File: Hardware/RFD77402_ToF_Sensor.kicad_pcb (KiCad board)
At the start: 2 copper layers, 25.4 x 25.4 mm, 18 parts, among them J1 QWIIC_CONNECTORJS-1MM, J2 QWIIC_CONNECTORJS-1MM, J3 CONN_01, J4 I2C_STANDARD, U1 RFD77402, U4 CC_LICENSE

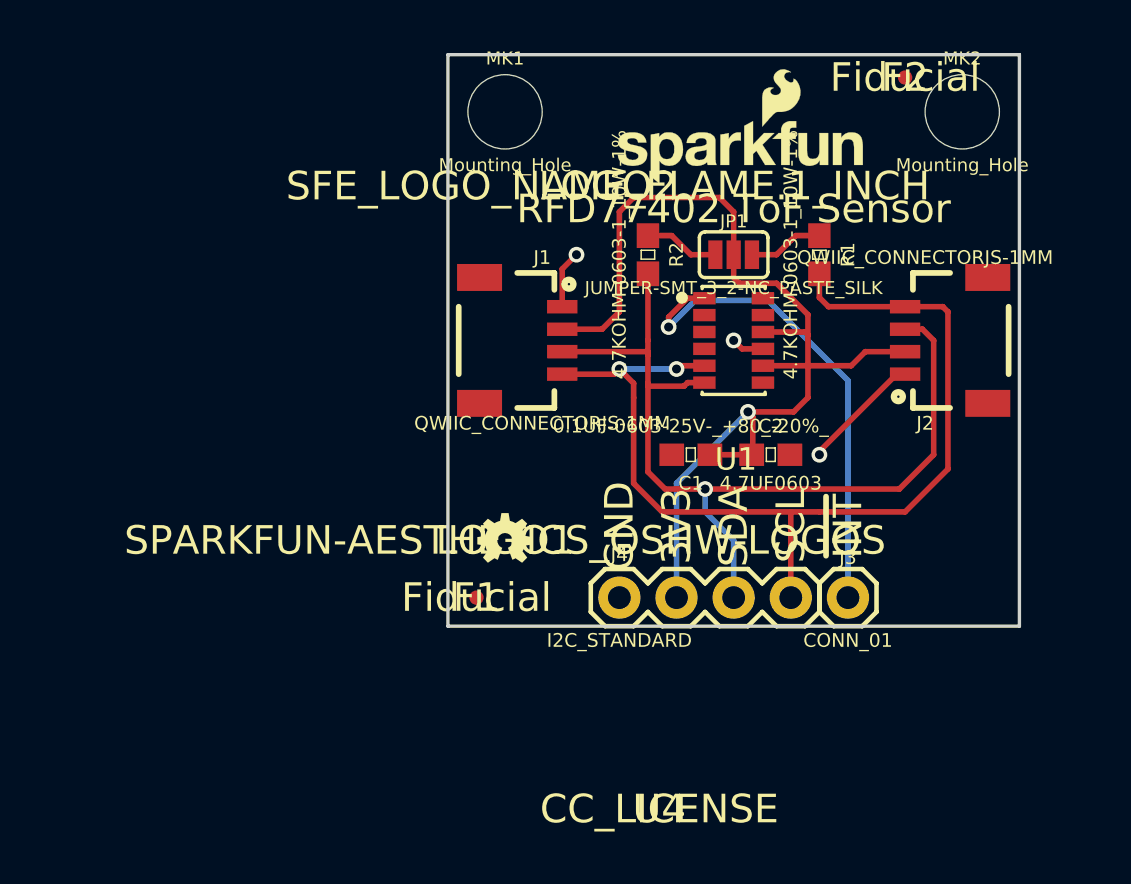
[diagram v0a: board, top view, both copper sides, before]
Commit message: Added fiducials
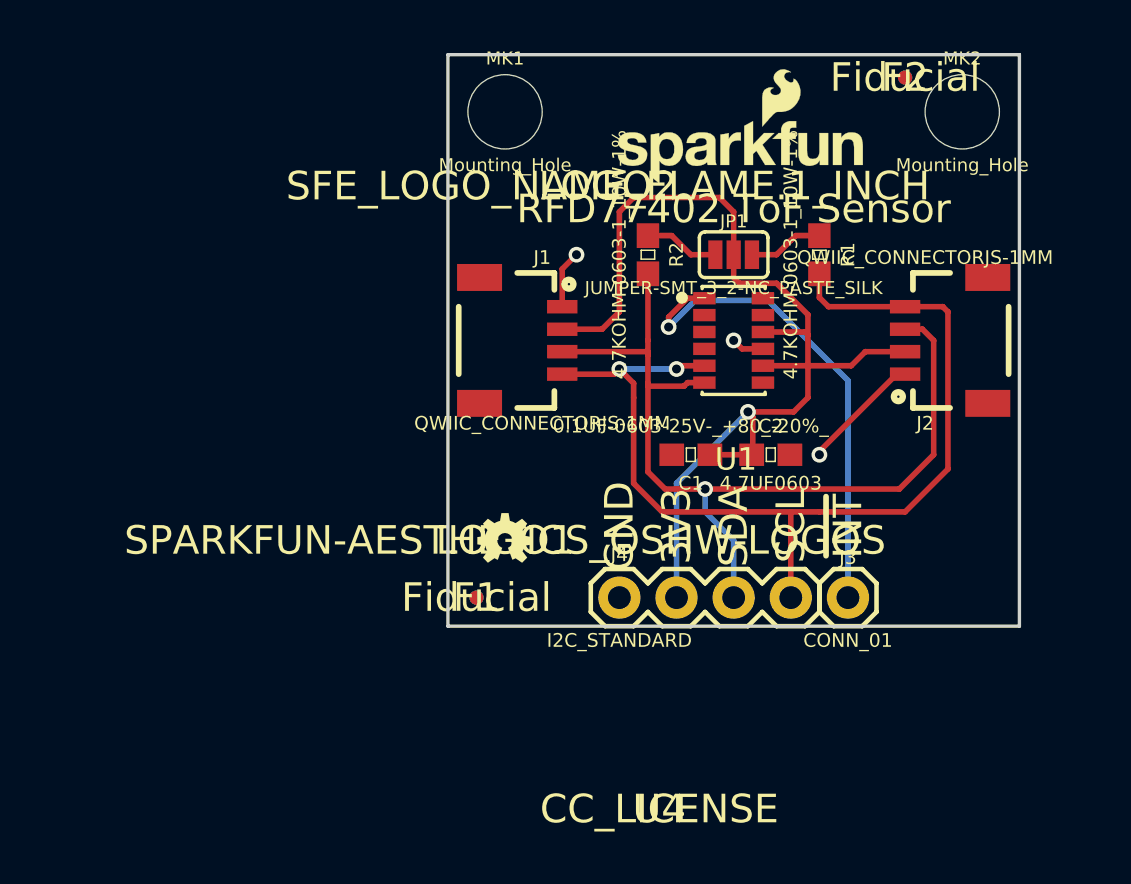
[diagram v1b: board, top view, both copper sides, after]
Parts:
- added F3: Fiducial, Aesthetics:FIDUCIAL-MICRO, B.Cu at (138.4, 115.6)
- added F4: Fiducial, Aesthetics:FIDUCIAL-MICRO, B.Cu at (157.5, 92.5)
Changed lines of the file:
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@@
     (tracks 96)
     (zones 0)
-    (modules 18)
+    (modules 20)
     (nets 8)
   )
@@
     (pad_to_mask_clearance 0.075)
     (aux_axis_origin 0 0)
-    (visible_elements 7FFCF3E9)
+    (visible_elements 7FFCF7E9)
     (pcbplotparams
       (layerselection 0x00030_80000001)
@@
       (net 1 GND))
   )
+  (module Aesthetics:FIDUCIAL-MICRO (layer B.Cu)
+    (at 138.43 115.57)
+    (descr "FIDUCIAL - CIRCLE, 0.25IN")
+    (tags "FIDUCIAL - CIRCLE, 0.25IN")
+    (attr smd)
+    (fp_text reference F3 (at 0 0) (layer B.SilkS)
+      (effects (font (thickness 0.15)) (justify mirror))
+    )
+    (fp_text value Fiducial (at 0 0) (layer B.SilkS)
+      (effects (font (thickness 0.15)) (justify mirror))
+    )
+    (pad 1 smd circle (at 0 0) (size 0.635 0.635) (layers B.Cu B.Paste B.Mask)
+      (solder_mask_margin 0.1016))
+  )
+  (module Aesthetics:FIDUCIAL-MICRO (layer B.Cu)
+    (at 157.48 92.456)
+    (descr "FIDUCIAL - CIRCLE, 0.25IN")
+    (tags "FIDUCIAL - CIRCLE, 0.25IN")
+    (attr smd)
+    (fp_text reference F4 (at 0 0) (layer B.SilkS)
+      (effects (font (thickness 0.15)) (justify mirror))
+    )
+    (fp_text value Fiducial (at 0 0) (layer B.SilkS)
+      (effects (font (thickness 0.15)) (justify mirror))
+    )
+    (pad 1 smd circle (at 0 0) (size 0.635 0.635) (layers B.Cu B.Paste B.Mask)
+      (solder_mask_margin 0.1016))
+  )
   (gr_text "RFD77402 ToF Sensor" (at 149.86 98.298) (layer B.SilkS)

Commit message: Post design review changes
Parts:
- added GND: VIA-15mil, Hardware:VIA-15mil, F.Cu at (159.8, 112.5)
- moved C1 1.53 mm to (147.8, 107.7)
- moved C2 1.53 mm to (151.4, 107.7)
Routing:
- net +3V3: track 48.5 -> 57.5 mm, vias 1 -> 2
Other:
- board text added: "Designed By: Nate Seidle Revised By: Andy England"
- board text added: "PU"
- board text added: "v01"
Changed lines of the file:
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@@
 (kicad_pcb (version 4) (host pcbnew 4.0.7)
   (general
-    (links 24)
+    (links 25)
     (no_connects 0)
-    (area 137.084999 91.364999 162.635001 116.915001)
+    (area 117.656001 90.922499 173.827142 126.4622)
     (thickness 1.6)
-    (drawings 16)
-    (tracks 96)
+    (drawings 22)
+    (tracks 104)
     (zones 0)
-    (modules 20)
+    (modules 21)
     (nets 8)
   )
@@
     (39 F.Mask user)
     (44 Edge.Cuts user)
-    (46 B.CrtYd user hide)
-    (47 F.CrtYd user hide)
+    (46 B.CrtYd user)
+    (47 F.CrtYd user)
     (48 B.Fab user hide)
     (49 F.Fab user)
@@
     (mod_text_size 1 1)
     (mod_text_width 0.15)
-    (pad_size 1.524 1.524)
-    (pad_drill 0.762)
+    (pad_size 0.6 0.6)
+    (pad_drill 0.3)
     (pad_to_mask_clearance 0.075)
     (aux_axis_origin 0 0)
-    (visible_elements 7FFCF7E9)
+    (visible_elements 7FFCFFEF)
     (pcbplotparams
       (layerselection 0x00030_80000001)
@@
   )
   (module Capacitors:0603 (layer F.Cu)
-    (at 147.955 109.22 180)
+    (at 147.828 107.696 180)
     (descr "GENERIC 1608 (0603) PACKAGE")
     (tags "GENERIC 1608 (0603) PACKAGE")
@@
   )
   (module Capacitors:0603 (layer F.Cu)
-    (at 151.51 109.22)
+    (at 151.384 107.696)
     (descr "GENERIC 1608 (0603) PACKAGE")
     (tags "GENERIC 1608 (0603) PACKAGE")
@@
       (solder_mask_margin 0.1016))
   )
+  (module Hardware:VIA-15mil (layer F.Cu)
+    (at 159.766 112.522)
+    (fp_text reference GND (at 0 0.5) (layer F.SilkS)
+      (effects (font (size 1 1) (thickness 0.15)))
+    )
+    (fp_text value VIA-15mil (at 0 -0.5) (layer F.Fab)
+      (effects (font (size 1 1) (thickness 0.15)))
+    )
+    (pad 1 thru_hole circle (at 0 0) (size 0.6 0.6) (drill 0.3) (layers *.Cu)
+      (net 1 GND) (zone_connect 2))
+  )
+  (gr_text PU (at 147.574 100.33 90) (layer F.SilkS)
+    (effects (font (size 1 1) (thickness 0.25)))
+  )
+  (gr_text "Designed By: Nate Seidle\nRevised By: Andy England" (at 148.844 121.412) (layer F.Fab)
+    (effects (font (size 1.27 1.27) (thickness 0.254)))
+  )
+  (dimension 25.4 (width 0.254) (layer F.Fab)
+    (gr_text "1 In" (at 134.239 104.14 270) (layer F.Fab)
+      (effects (font (size 1.27 1.27) (thickness 0.254)))
+    )
+    (feature1 (pts (xy 137.16 116.84) (xy 133.096 116.84)))
+    (feature2 (pts (xy 137.16 91.44) (xy 133.096 91.44)))
+    (crossbar (pts (xy 135.382 91.44) (xy 135.382 116.84)))
+    (arrow1a (pts (xy 135.382 116.84) (xy 134.795579 115.713496)))
+    (arrow1b (pts (xy 135.382 116.84) (xy 135.968421 115.713496)))
+    (arrow2a (pts (xy 135.382 91.44) (xy 134.795579 92.566504)))
+    (arrow2b (pts (xy 135.382 91.44) (xy 135.968421 92.566504)))
+  )
+  (dimension 20.32 (width 0.254) (layer F.Fab)
+    (gr_text ".8 In" (at 149.86 88.773001) (layer F.Fab)
+      (effects (font (size 1.27 1.27) (thickness 0.254)))
+    )
+    (feature1 (pts (xy 139.7 93.98) (xy 139.7 87.630001)))
+    (feature2 (pts (xy 160.02 93.98) (xy 160.02 87.630001)))
+    (crossbar (pts (xy 160.02 89.916001) (xy 139.7 89.916001)))
+    (arrow1a (pts (xy 139.7 89.916001) (xy 140.826504 89.32958)))
+    (arrow1b (pts (xy 139.7 89.916001) (xy 140.826504 90.502422)))
+    (arrow2a (pts (xy 160.02 89.916001) (xy 158.893496 89.32958)))
+    (arrow2b (pts (xy 160.02 89.916001) (xy 158.893496 90.502422)))
+  )
+  (dimension 25.4 (width 0.254) (layer F.Fab)
+    (gr_text "1 In" (at 149.86 85.471) (layer F.Fab)
+      (effects (font (size 1.27 1.27) (thickness 0.254)))
+    )
+    (feature1 (pts (xy 162.56 91.186) (xy 162.56 84.328)))
+    (feature2 (pts (xy 137.16 91.186) (xy 137.16 84.328)))
+    (crossbar (pts (xy 137.16 86.614) (xy 162.56 86.614)))
+    (arrow1a (pts (xy 162.56 86.614) (xy 161.433496 87.200421)))
+    (arrow1b (pts (xy 162.56 86.614) (xy 161.433496 86.027579)))
+    (arrow2a (pts (xy 137.16 86.614) (xy 138.286504 87.200421)))
+    (arrow2b (pts (xy 137.16 86.614) (xy 138.286504 86.027579)))
+  )
+  (gr_text v01 (at 160.528 115.57) (layer B.Cu)
+    (effects (font (size 1.27 1.27) (thickness 0.254)) (justify mirror))
+  )
   (gr_text "RFD77402 ToF Sensor" (at 149.86 98.298) (layer B.SilkS)
     (effects (font (size 1.27 1.27) (thickness 0.254)) (justify mirror))
@@
   (via (at 142.875 100.33) (size 0.7) (drill 0.4) (layers F.Cu B.Cu) (net 1))
   (segment (start 142.24 100.965) (end 142.875 100.33) (width 0.25) (layer F.Cu) (net 1))
-  (segment (start 148.805 109.22) (end 150.66 109.22) (width 0.25) (layer F.Cu) (net 2))
-  (segment (start 153.162 106.68) (end 153.162 105.265) (width 0.25) (layer F.Cu) (net 2))
-  (segment (start 150.495 107.315) (end 152.527 107.315) (width 0.25) (layer F.Cu) (net 2))
-  (segment (start 152.527 107.315) (end 153.162 106.68) (width 0.25) (layer F.Cu) (net 2))
+  (segment (start 142.24 103.64216) (end 140.95984 103.64216) (width 0.25) (layer F.Cu) (net 2))
+  (segment (start 143.256 112.014) (end 147.32 112.014) (width 0.25) (layer B.Cu) (net 2))
+  (via (at 143.256 112.014) (size 0.7) (drill 0.4) (layers F.Cu B.Cu) (net 2))
+  (segment (start 142.748 112.014) (end 143.256 112.014) (width 0.25) (layer F.Cu) (net 2))
+  (segment (start 140.462 109.728) (end 142.748 112.014) (width 0.25) (layer F.Cu) (net 2))
+  (segment (start 140.462 104.14) (end 140.462 109.728) (width 0.25) (layer F.Cu) (net 2))
+  (segment (start 140.95984 103.64216) (end 140.462 104.14) (width 0.25) (layer F.Cu) (net 2))
+  (segment (start 149.098 108.966) (end 150.114 108.966) (width 0.25) (layer F.Cu) (net 2))
+  (segment (start 150.53564 108.54436) (end 150.53564 107.696) (width 0.25) (layer F.Cu) (net 2))
+  (segment (start 150.114 108.966) (end 150.53564 108.54436) (width 0.25) (layer F.Cu) (net 2))
+  (segment (start 149.098 108.966) (end 148.844 108.966) (width 0.25) (layer F.Cu) (net 2))
+  (segment (start 148.844 108.966) (end 148.67636 108.79836) (width 0.25) (layer F.Cu) (net 2))
+  (segment (start 148.67636 108.79836) (end 148.67636 107.696) (width 0.25) (layer F.Cu) (net 2))
+  (segment (start 147.32 115.57) (end 147.32 112.014) (width 0.25) (layer B.Cu) (net 2))
+  (segment (start 147.32 112.014) (end 147.32 110.744) (width 0.25) (layer B.Cu) (net 2))
+  (segment (start 147.32 110.744) (end 149.098 108.966) (width 0.25) (layer B.Cu) (net 2))
+  (via (at 149.098 108.966) (size 0.7) (drill 0.4) (layers F.Cu B.Cu) (net 2))
   (segment (start 149.86 100.33) (end 149.86 101.346) (width 0.25) (layer F.Cu) (net 2))
   (segment (start 149.86 101.346) (end 150.114 101.6) (width 0.25) (layer F.Cu) (net 2))
@@
   (segment (start 151.16 103.765) (end 153.041 103.765) (width 0.25) (layer F.Cu) (net 2))
   (segment (start 153.041 103.765) (end 153.162 103.886) (width 0.25) (layer F.Cu) (net 2))
-  (segment (start 150.71 109.22) (end 150.71 107.53) (width 0.25) (layer F.Cu) (net 2))
-  (segment (start 150.71 107.53) (end 150.495 107.315) (width 0.25) (layer F.Cu) (net 2))
   (segment (start 151.16 105.265) (end 153.162 105.265) (width 0.25) (layer F.Cu) (net 2))
   (segment (start 153.162 105.265) (end 155.085 105.265) (width 0.25) (layer F.Cu) (net 2))
   (segment (start 155.085 105.265) (end 155.71 104.64) (width 0.25) (layer F.Cu) (net 2))
   (segment (start 155.71 104.64) (end 157.48 104.64) (width 0.25) (layer F.Cu) (net 2))
-  (segment (start 147.32 115.57) (end 147.32 110.49) (width 0.25) (layer B.Cu) (net 2))
-  (via (at 150.495 107.315) (size 0.7) (drill 0.4) (layers F.Cu B.Cu) (net 2))
-  (segment (start 147.32 110.49) (end 150.495 107.315) (width 0.25) (layer B.Cu) (net 2))
   (segment (start 146.812 110.744) (end 148.59 110.744) (width 0.25) (layer F.Cu) (net 3))
   (segment (start 148.59 110.744) (end 157.226 110.744) (width 0.25) (layer F.Cu) (net 3))

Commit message: Post checklist changes
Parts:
- added GND: VIA-15mil, Hardware:VIA-15mil, F.Cu at (139.4, 99.6)
- moved R1 1.02 mm to (154.7, 100.3), turned to 0 degrees
- moved R2 1.02 mm to (145.0, 100.3), turned to 180 degrees
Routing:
- net +3V3: track 57.5 -> 60.0 mm
- net SCL: track 44.9 -> 43.7 mm

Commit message: post design review changes
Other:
- board text added: "I2C-0x4C"
- board text added: "v02"
- board text removed: "v01"
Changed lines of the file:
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@@
   (general
     (links 26)
-    (no_connects 1)
+    (no_connects 0)
     (area 117.656001 84.328 173.827142 126.4622)
     (thickness 1.6)
-    (drawings 22)
+    (drawings 23)
     (tracks 100)
     (zones 0)
@@
       (net 1 GND) (zone_connect 2))
   )
+  (gr_text I2C-0x4C (at 149.86 106.68) (layer B.SilkS)
+    (effects (font (size 1.27 1.27) (thickness 0.254)) (justify mirror))
+  )
   (gr_text PU (at 147.574 100.33 90) (layer F.SilkS)
     (effects (font (size 1 1) (thickness 0.25)))
@@
     (arrow2b (pts (xy 137.16 86.614) (xy 138.286504 86.027579)))
   )
-  (gr_text v01 (at 160.528 115.57) (layer B.Cu)
+  (gr_text v02 (at 160.528 115.57) (layer B.Cu)
     (effects (font (size 1.27 1.27) (thickness 0.254)) (justify mirror))
   )

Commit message: post design review changes
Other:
- board text added: "v10"
- board text removed: "v02"
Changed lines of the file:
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@@
     (arrow2b (pts (xy 137.16 86.614) (xy 138.286504 86.027579)))
   )
-  (gr_text v02 (at 160.528 115.57) (layer B.Cu)
+  (gr_text v10 (at 160.528 115.57) (layer B.Cu)
     (effects (font (size 1.27 1.27) (thickness 0.254)) (justify mirror))
   )
@@
     (effects (font (size 1.27 1.27) (thickness 0.254)) (justify mirror))
   )
-  (gr_text GND (at 144.78 112.395 90) (layer B.SilkS)
+  (gr_text GND (at 144.78 112.268 90) (layer B.SilkS)
     (effects (font (size 1.27 1.27) (thickness 0.254)) (justify mirror))
   )
@@
     (effects (font (size 1.27 1.27) (thickness 0.254)))
   )
-  (gr_text GND (at 144.78 112.395 90) (layer F.SilkS)
+  (gr_text GND (at 144.78 112.268 90) (layer F.SilkS)
     (effects (font (size 1.27 1.27) (thickness 0.254)))
   )
